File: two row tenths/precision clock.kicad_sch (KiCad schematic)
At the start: 56 parts, among them P1 USB_C_Plug_USB2.0, P2 USB_C_Plug_USB2.0, Q1 MMBT3906, Q2 MMBT3906

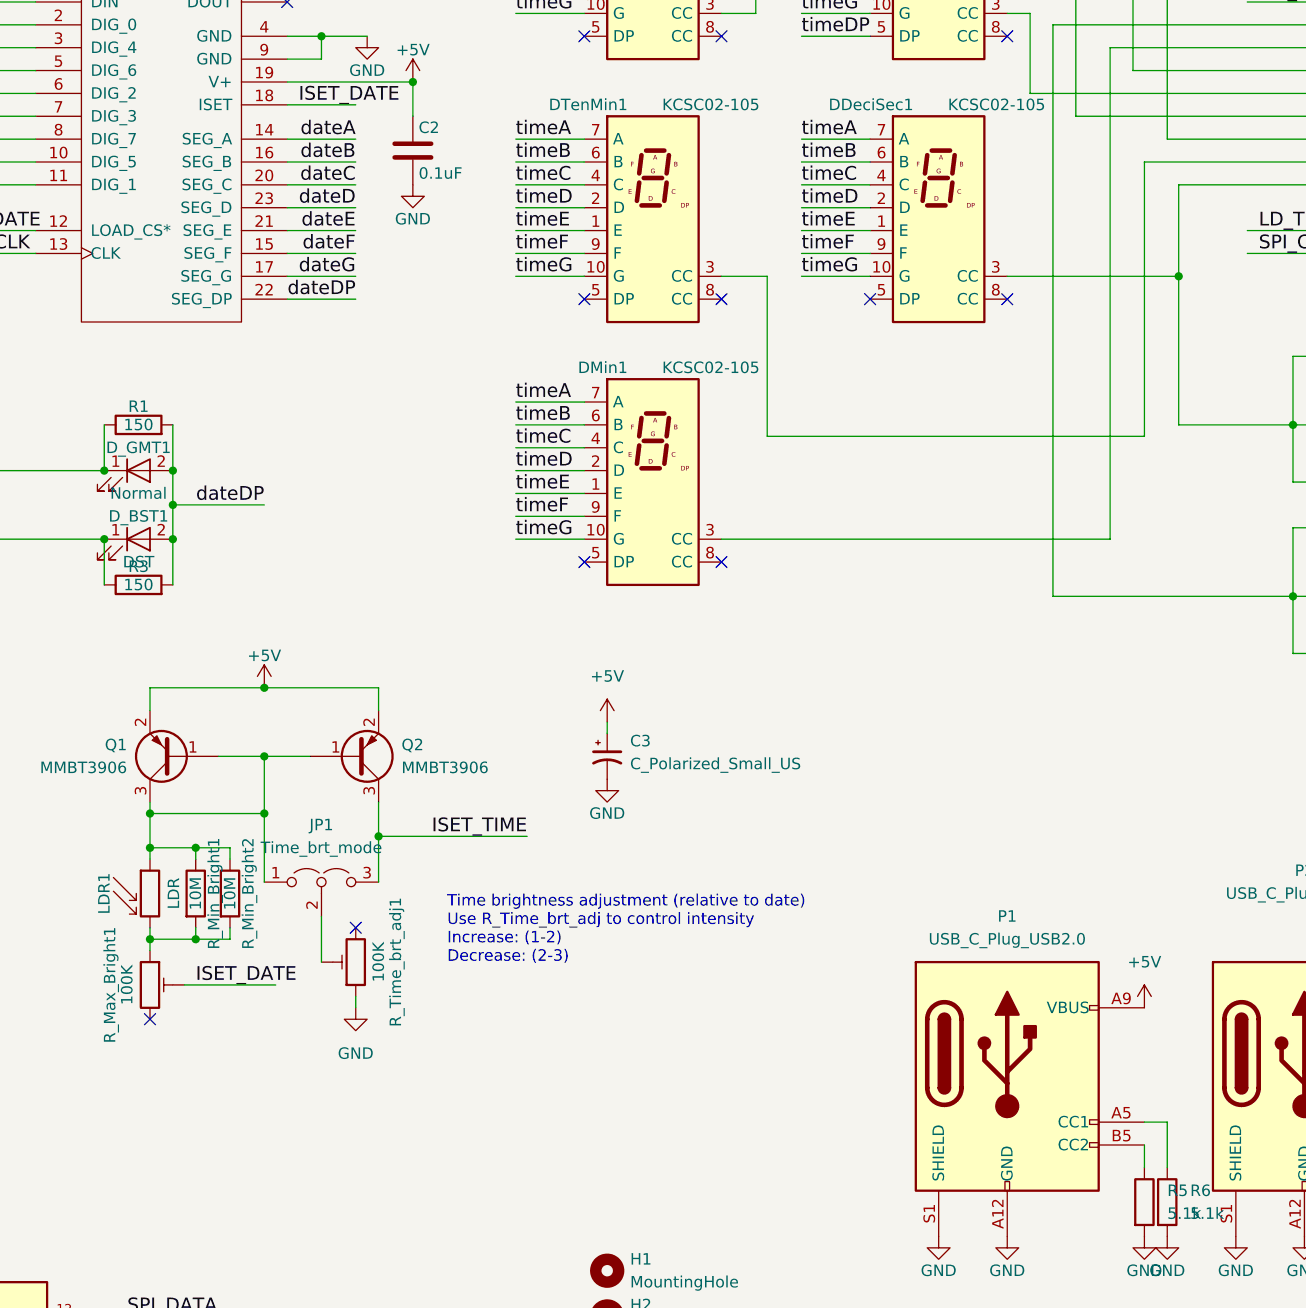
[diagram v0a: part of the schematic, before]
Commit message: Add resistor so we don't short Q2
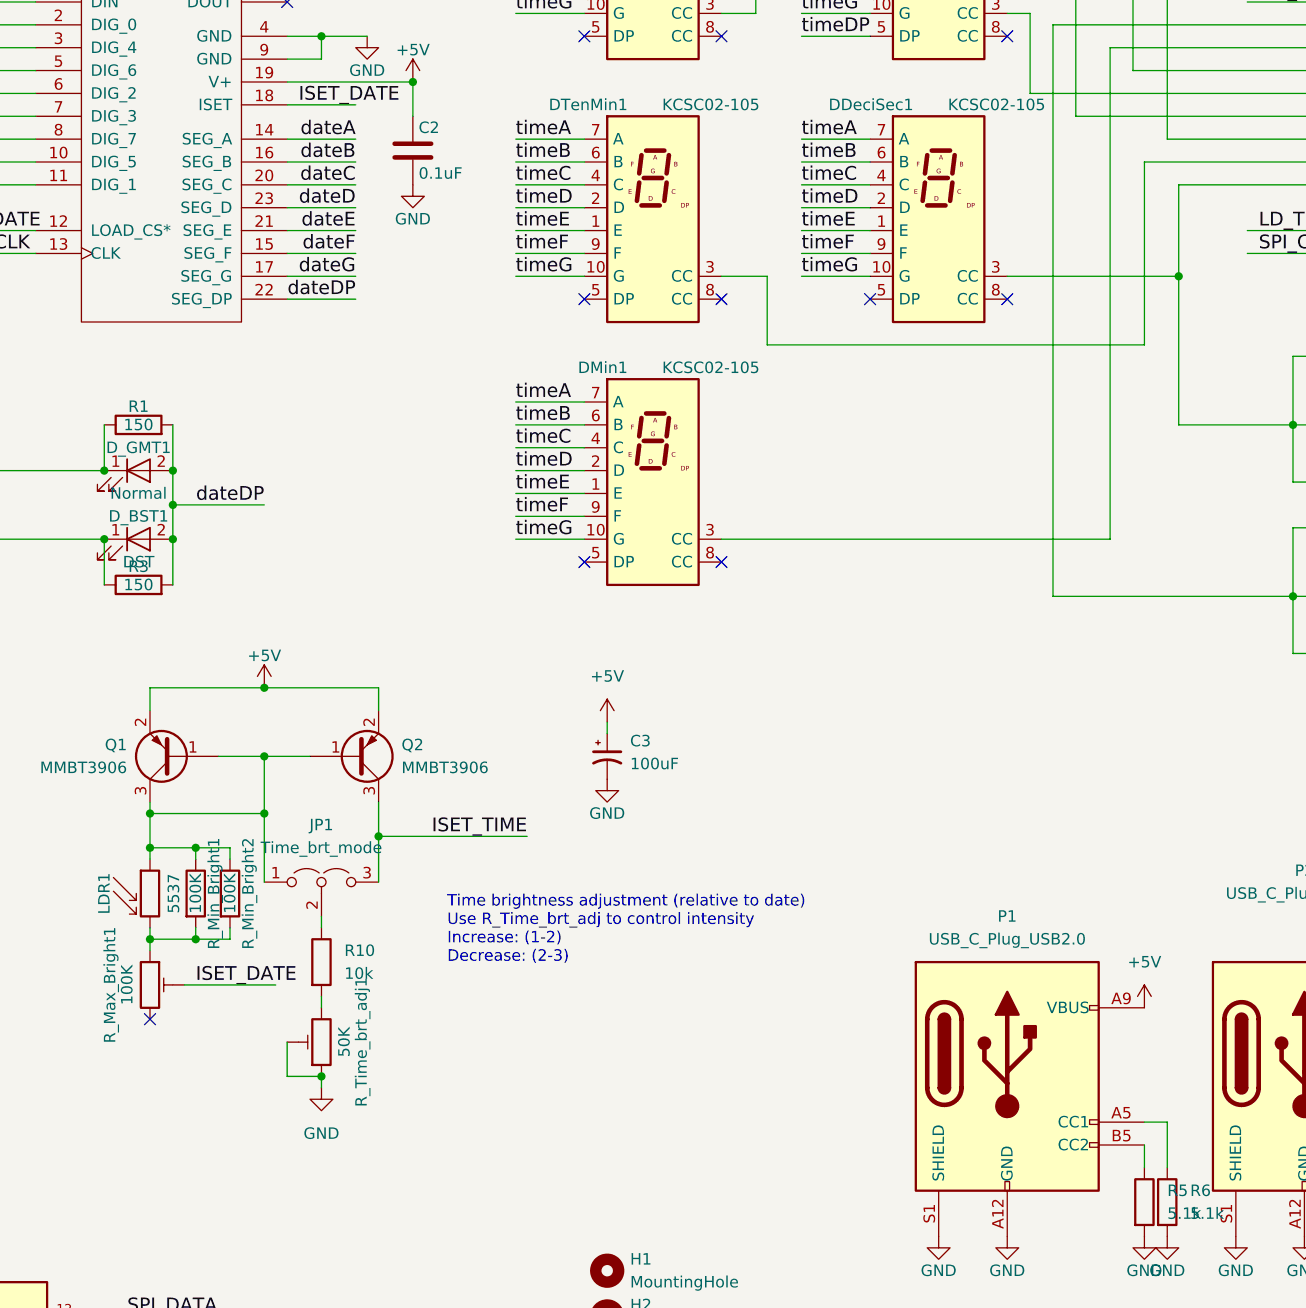
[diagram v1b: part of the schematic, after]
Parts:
- added R10: 10k, Resistor_SMD:R_1206_3216Metric, symbol Device:R
- C3: value C_Polarized_Small_US -> 100uF
- LDR1: value LDR -> 5537
- R_Min_Bright1, R_Min_Bright2: value 10M -> 100K
- R_Time_brt_adj1: value 100K -> 50K
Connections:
- net GND: now also R_Time_brt_adj1.2
- net at JP1.2 (C): now also R10.1; no longer R_Time_brt_adj1.2
- net at R_Time_brt_adj1.3: now also R10.2
- no-connect marks 59 -> 58
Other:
- moved on the sheet: R_Time_brt_adj1
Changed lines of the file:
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@@
 	)
 	(junction
+		(at 140.97 185.42)
+		(diameter 0)
+		(color 0 0 0 0)
+	)
+	(junction
 		(at 285.75 69.85)
 		(diameter 0)
@@
 	)
 	(no_connect
-		(at 144.78 168.91)
-	)
-	(no_connect
 		(at 63.5 146.05)
 	)
@@
 	(wire
 		(pts
-			(xy 50.8 133.35) (xy 50.8 158.75)
+			(xy 140.97 177.8) (xy 140.97 176.53)
 		)
 		(stroke
@@
 	(wire
 		(pts
-			(xy 63.5 120.65) (xy 55.88 120.65)
+			(xy 50.8 133.35) (xy 50.8 158.75)
 		)
 		(stroke
@@
 	(wire
 		(pts
-			(xy 190.5 96.52) (xy 190.5 114.3)
+			(xy 63.5 120.65) (xy 55.88 120.65)
 		)
 		(stroke
@@
 	(wire
 		(pts
-			(xy 140.97 167.64) (xy 140.97 172.72)
+			(xy 190.5 96.52) (xy 190.5 104.14)
 		)
 		(stroke
@@
 	(wire
 		(pts
-			(xy 232.41 83.82) (xy 232.41 114.3)
+			(xy 232.41 83.82) (xy 232.41 104.14)
 		)
 		(stroke
@@
 	(wire
 		(pts
+			(xy 137.16 181.61) (xy 137.16 185.42)
+		)
+		(stroke
+			(width 0)
+			(type default)
+		)
+	)
+	(wire
+		(pts
 			(xy 129.54 149.86) (xy 134.62 149.86)
 		)
@@
 	(wire
 		(pts
+			(xy 140.97 168.91) (xy 140.97 167.64)
+		)
+		(stroke
+			(width 0)
+			(type default)
+		)
+	)
+	(wire
+		(pts
 			(xy 137.16 69.85) (xy 140.97 69.85)
 		)
@@
 	(wire
 		(pts
+			(xy 137.16 185.42) (xy 140.97 185.42)
+		)
+		(stroke
+			(width 0)
+			(type default)
+		)
+	)
+	(wire
+		(pts
 			(xy 31.75 96.52) (xy 24.13 96.52)
 		)
@@
 	(wire
 		(pts
-			(xy 144.78 176.53) (xy 144.78 177.8)
+			(xy 140.97 185.42) (xy 140.97 186.69)
 		)
 		(stroke
@@
 	(wire
 		(pts
-			(xy 190.5 114.3) (xy 232.41 114.3)
+			(xy 190.5 104.14) (xy 232.41 104.14)
 		)
 		(stroke
@@
 			)
 		)
-		(property "Value" "LDR"
+		(property "Value" "5537"
 			(at 123.825 165.1 90)
 			(effects
@@
 			)
 		)
-		(property "Value" "10M"
+		(property "Value" "100K"
 			(at 127 165.1 90)
 			(effects
@@
 	(symbol
 		(lib_id "precision-clock-rescue:POT_TRIM")
-		(at 144.78 172.72 180)
+		(at 140.97 181.61 180)
 		(unit 1)
 		(exclude_from_sim no)
@@
 		(dnp no)
 		(property "Reference" "R_Time_brt_adj1"
-			(at 149.225 172.72 90)
+			(at 145.415 181.61 90)
 			(effects
 				(font
@@
 			)
 		)
-		(property "Value" "100K"
-			(at 147.32 172.72 90)
+		(property "Value" "50K"
+			(at 143.51 181.61 90)
 			(effects
 				(font
@@
 		)
 		(property "Footprint" "Potentiometer_THT:Potentiometer_Piher_PT-6-V_Vertical"
-			(at 144.78 172.72 0)
+			(at 140.97 181.61 0)
 			(effects
 				(font
@@
 		)
 		(property "Datasheet" ""
-			(at 144.78 172.72 0)
+			(at 140.97 181.61 0)
 			(effects
 				(font
@@
 		)
 		(property "Description" ""
-			(at 144.78 172.72 0)
+			(at 140.97 181.61 0)
 			(effects
 				(font
@@
 			)
 		)
-		(property "Value" "10M"
+		(property "Value" "100K"
 			(at 130.81 165.1 90)
 			(effects
@@
 	)
 	(symbol
+		(lib_id "Device:R")
+		(at 140.97 172.72 0)
+		(unit 1)
+		(exclude_from_sim no)
+		(in_bom yes)
+		(on_board yes)
+		(dnp no)
+		(fields_autoplaced yes)
+		(property "Reference" "R10"
+			(at 143.51 171.4499 0)
+			(effects
+				(font
+					(size 1.27 1.27)
+				)
+				(justify left)
+			)
+		)
+		(property "Value" "10k"
+			(at 143.51 173.9899 0)
+			(effects
+				(font
+					(size 1.27 1.27)
+				)
+				(justify left)
+			)
+		)
+		(property "Footprint" "Resistor_SMD:R_1206_3216Metric"
+			(at 139.192 172.72 90)
+			(effects
+				(font
+					(size 1.27 1.27)
+				)
+				(hide yes)
+			)
+		)
+		(property "Datasheet" "~"
+			(at 140.97 172.72 0)
+			(effects
+				(font
+					(size 1.27 1.27)
+				)
+				(hide yes)
+			)
+		)
+		(property "Description" "Resistor"
+			(at 140.97 172.72 0)
+			(effects
+				(font
+					(size 1.27 1.27)
+				)
+				(hide yes)
+			)
+		)
+		(pin "1"
+		)
+		(pin "2"
+		)
+		(instances
+			(project ""
+				(path "/a352d3ae-caca-4fe6-94e2-4912021cb238"
+					(reference "R10")
+					(unit 1)
+				)
+			)
+		)
+	)
+	(symbol
 		(lib_id "Connector:USB_C_Receptacle_PowerOnly_6P")
 		(at 250.19 185.42 0)
@@
 	(symbol
 		(lib_id "power:GND")
-		(at 144.78 177.8 0)
+		(at 140.97 186.69 0)
 		(unit 1)
 		(exclude_from_sim no)
@@
 		(fields_autoplaced yes)
 		(property "Reference" "#PWR010"
-			(at 144.78 184.15 0)
+			(at 140.97 193.04 0)
 			(effects
 				(font
@@
 		)
 		(property "Value" "GND"
-			(at 144.78 182.88 0)
+			(at 140.97 191.77 0)
 			(effects
 				(font
@@
 		)
 		(property "Footprint" ""
-			(at 144.78 177.8 0)
+			(at 140.97 186.69 0)
 			(effects
 				(font
@@
 		)
 		(property "Datasheet" ""
-			(at 144.78 177.8 0)
+			(at 140.97 186.69 0)
 			(effects
 				(font
@@
 		)
 		(property "Description" "Power symbol creates a global label with name \"GND\" , ground"
-			(at 144.78 177.8 0)
+			(at 140.97 186.69 0)
 			(effects
 				(font
@@
 			)
 		)
-		(property "Value" "C_Polarized_Small_US"
+		(property "Value" "100uF"
 			(at 175.26 150.6981 0)
 			(effects

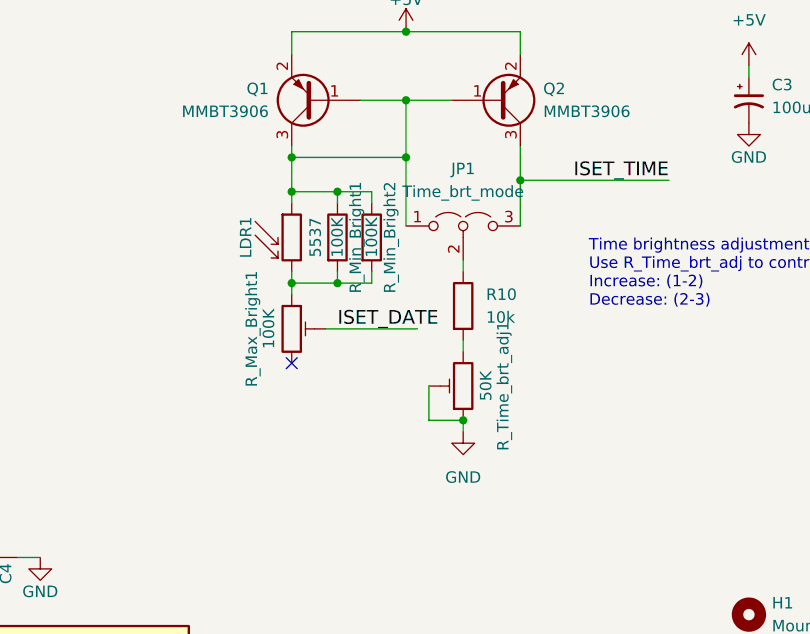
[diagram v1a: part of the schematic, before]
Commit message: More resistors for brightness tuning
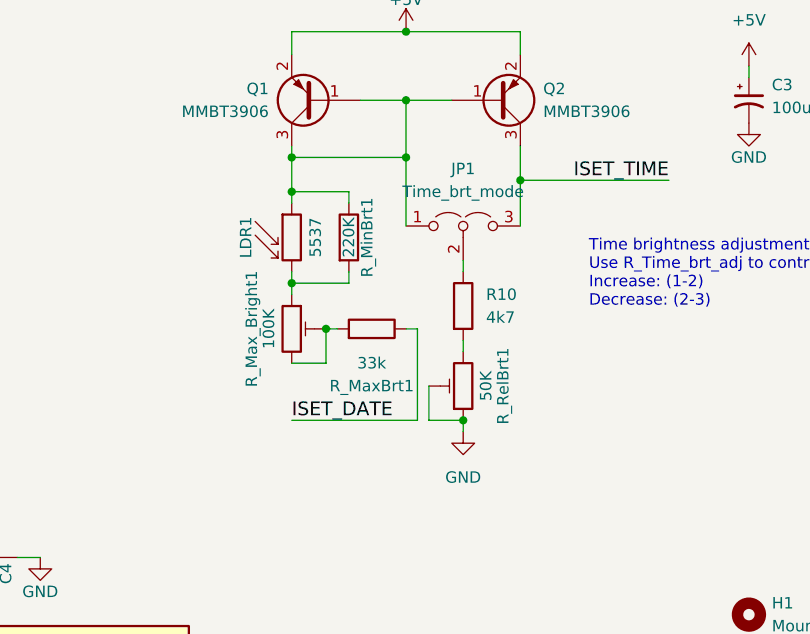
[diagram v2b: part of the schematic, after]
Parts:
- removed R_Min_Bright1: 100K, Resistor_THT:R_Axial_DIN0207_L6.3mm_D2.5mm_P7.62mm_Horizontal, symbol precision-clock-rescue:R
- added R_MaxBrt1: 33k, Resistor_SMD:R_1206_3216Metric, symbol Device:R
- R10: value 10k -> 4k7
- R_MinBrt1: renamed from R_Min_Bright2; value 100K -> 220K
- renumbered R_Time_brt_adj1 to R_RelBrt1
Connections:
- net ISET_DATE: now also R_MaxBrt1.1; no longer R_Max_Bright1.2
- net at R_Max_Bright1.3: now also R_Max_Bright1.2, R_MaxBrt1.2
- no-connect marks 58 -> 57
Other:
- moved on the sheet: R_MinBrt1
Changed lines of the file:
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@@
 	)
 	(junction
-		(at 127 160.02)
-		(diameter 0)
-		(color 0 0 0 0)
-	)
-	(junction
 		(at 83.82 125.73)
 		(diameter 0)
@@
 	)
 	(junction
-		(at 127 170.18)
+		(at 50.8 133.35)
 		(diameter 0)
 		(color 0 0 0 0)
 	)
 	(junction
-		(at 50.8 133.35)
+		(at 140.97 69.85)
 		(diameter 0)
 		(color 0 0 0 0)
 	)
 	(junction
-		(at 140.97 69.85)
+		(at 125.73 175.26)
 		(diameter 0)
 		(color 0 0 0 0)
@@
 	)
 	(no_connect
-		(at 121.92 179.07)
-	)
-	(no_connect
 		(at 31.75 99.06)
 	)
@@
 	(wire
 		(pts
+			(xy 135.89 185.42) (xy 121.92 185.42)
+		)
+		(stroke
+			(width 0)
+			(type default)
+		)
+	)
+	(wire
+		(pts
 			(xy 209.55 240.03) (xy 196.85 240.03)
 		)
@@
 	(wire
 		(pts
+			(xy 135.89 175.26) (xy 135.89 185.42)
+		)
+		(stroke
+			(width 0)
+			(type default)
+		)
+	)
+	(wire
+		(pts
 			(xy 121.92 168.91) (xy 121.92 170.18)
 		)
@@
 	(wire
 		(pts
-			(xy 127 160.02) (xy 130.81 160.02)
-		)
-		(stroke
-			(width 0)
-			(type default)
-		)
-	)
-	(wire
-		(pts
 			(xy 96.52 81.28) (xy 96.52 15.24)
 		)
@@
 	(wire
 		(pts
-			(xy 127 170.18) (xy 121.92 170.18)
+			(xy 121.92 170.18) (xy 128.27 170.18)
 		)
 		(stroke
@@
 	(wire
 		(pts
-			(xy 127 160.02) (xy 121.92 160.02)
+			(xy 121.92 160.02) (xy 128.27 160.02)
 		)
 		(stroke
@@
 	(wire
 		(pts
-			(xy 130.81 170.18) (xy 127 170.18)
+			(xy 135.89 175.26) (xy 134.62 175.26)
 		)
 		(stroke
@@
 	(wire
 		(pts
-			(xy 125.73 175.26) (xy 135.89 175.26)
-		)
-		(stroke
-			(width 0)
-			(type default)
-		)
-	)
-	(wire
-		(pts
 			(xy 147.32 154.94) (xy 147.32 158.75)
 		)
@@
 	(wire
 		(pts
-			(xy 127 161.29) (xy 127 160.02)
+			(xy 189.23 15.24) (xy 189.23 38.1)
 		)
 		(stroke
@@
 	(wire
 		(pts
-			(xy 189.23 15.24) (xy 189.23 38.1)
+			(xy 170.18 91.44) (xy 162.56 91.44)
 		)
 		(stroke
@@
 	(wire
 		(pts
-			(xy 170.18 91.44) (xy 162.56 91.44)
+			(xy 125.73 175.26) (xy 125.73 179.07)
 		)
 		(stroke
@@
 	(wire
 		(pts
-			(xy 236.22 113.03) (xy 248.92 113.03)
+			(xy 125.73 175.26) (xy 127 175.26)
 		)
 		(stroke
@@
 	(wire
 		(pts
-			(xy 31.75 158.75) (xy 24.13 158.75)
+			(xy 236.22 113.03) (xy 248.92 113.03)
 		)
 		(stroke
@@
 	(wire
 		(pts
-			(xy 63.5 59.69) (xy 55.88 59.69)
+			(xy 31.75 158.75) (xy 24.13 158.75)
 		)
 		(stroke
@@
 	(wire
 		(pts
-			(xy 127 168.91) (xy 127 170.18)
+			(xy 63.5 59.69) (xy 55.88 59.69)
 		)
 		(stroke
@@
 	(wire
 		(pts
-			(xy 130.81 168.91) (xy 130.81 170.18)
+			(xy 128.27 168.91) (xy 128.27 170.18)
 		)
 		(stroke
@@
 	(wire
 		(pts
+			(xy 125.73 179.07) (xy 121.92 179.07)
+		)
+		(stroke
+			(width 0)
+			(type default)
+		)
+	)
+	(wire
+		(pts
 			(xy 281.94 77.47) (xy 289.56 77.47)
 		)
@@
 	(wire
 		(pts
-			(xy 130.81 161.29) (xy 130.81 160.02)
+			(xy 128.27 161.29) (xy 128.27 160.02)
 		)
 		(stroke
@@
 	)
 	(label "ISET_DATE"
-		(at 127 175.26 0)
+		(at 121.92 185.42 0)
 		(fields_autoplaced yes)
 		(effects
@@
 	)
 	(symbol
-		(lib_id "precision-clock-rescue:R")
-		(at 127 165.1 0)
-		(unit 1)
-		(exclude_from_sim no)
-		(in_bom yes)
-		(on_board yes)
-		(dnp no)
-		(property "Reference" "R_Min_Bright1"
-			(at 129.032 165.1 90)
-			(effects
-				(font
-					(size 1.27 1.27)
-				)
-			)
-		)
-		(property "Value" "100K"
-			(at 127 165.1 90)
-			(effects
-				(font
-					(size 1.27 1.27)
-				)
-			)
-		)
-		(property "Footprint" "Resistor_THT:R_Axial_DIN0207_L6.3mm_D2.5mm_P7.62mm_Horizontal"
-			(at 125.222 165.1 90)
-			(effects
-				(font
-					(size 1.27 1.27)
-				)
-				(hide yes)
-			)
-		)
-		(property "Datasheet" ""
-			(at 127 165.1 0)
-			(effects
-				(font
-					(size 1.27 1.27)
-				)
-				(hide yes)
-			)
-		)
-		(property "Description" ""
-			(at 127 165.1 0)
-			(effects
-				(font
-					(size 1.27 1.27)
-				)
-				(hide yes)
-			)
-		)
-		(pin "2"
-		)
-		(pin "1"
-		)
-		(instances
-			(project ""
-				(path "/a352d3ae-caca-4fe6-94e2-4912021cb238"
-					(reference "R_Min_Bright1")
-					(unit 1)
-				)
-			)
-		)
-	)
-	(symbol
 		(lib_id "precision-clock-rescue:NEO6MV2")
 		(at 231.14 213.36 0)
@@
 		(on_board yes)
 		(dnp no)
-		(property "Reference" "R_Time_brt_adj1"
+		(property "Reference" "R_RelBrt1"
 			(at 145.415 181.61 90)
 			(effects
@@
 			(project "precision clock"
 				(path "/a352d3ae-caca-4fe6-94e2-4912021cb238"
-					(reference "R_Time_brt_adj1")
+					(reference "R_RelBrt1")
 					(unit 1)
 				)
@@
 	(symbol
 		(lib_id "precision-clock-rescue:R")
-		(at 130.81 165.1 0)
+		(at 128.27 165.1 0)
 		(unit 1)
 		(exclude_from_sim no)
@@
 		(on_board yes)
 		(dnp no)
-		(property "Reference" "R_Min_Bright2"
-			(at 132.842 165.1 90)
+		(property "Reference" "R_MinBrt1"
+			(at 130.302 165.1 90)
 			(effects
 				(font
@@
 			)
 		)
-		(property "Value" "100K"
-			(at 130.81 165.1 90)
+		(property "Value" "220K"
+			(at 128.27 165.1 90)
 			(effects
 				(font
@@
 		)
 		(property "Footprint" "Resistor_SMD:R_1206_3216Metric"
-			(at 129.032 165.1 90)
+			(at 126.492 165.1 90)
 			(effects
 				(font
@@
 		)
 		(property "Datasheet" ""
-			(at 130.81 165.1 0)
+			(at 128.27 165.1 0)
 			(effects
 				(font
@@
 		)
 		(property "Description" ""
-			(at 130.81 165.1 0)
+			(at 128.27 165.1 0)
 			(effects
 				(font
@@
 			(project "precision clock"
 				(path "/a352d3ae-caca-4fe6-94e2-4912021cb238"
-					(reference "R_Min_Bright2")
+					(reference "R_MinBrt1")
 					(unit 1)
 				)
@@
 	)
 	(symbol
+		(lib_id "Device:R")
+		(at 130.81 175.26 270)
+		(mirror x)
+		(unit 1)
+		(exclude_from_sim no)
+		(in_bom yes)
+		(on_board yes)
+		(dnp no)
+		(property "Reference" "R_MaxBrt1"
+			(at 130.81 181.61 90)
+			(effects
+				(font
+					(size 1.27 1.27)
+				)
+			)
+		)
+		(property "Value" "33k"
+			(at 130.81 179.07 90)
+			(effects
+				(font
+					(size 1.27 1.27)
+				)
+			)
+		)
+		(property "Footprint" "Resistor_SMD:R_1206_3216Metric"
+			(at 130.81 177.038 90)
+			(effects
+				(font
+					(size 1.27 1.27)
+				)
+				(hide yes)
+			)
+		)
+		(property "Datasheet" "~"
+			(at 130.81 175.26 0)
+			(effects
+				(font
+					(size 1.27 1.27)
+				)
+				(hide yes)
+			)
+		)
+		(property "Description" "Resistor"
+			(at 130.81 175.26 0)
+			(effects
+				(font
+					(size 1.27 1.27)
+				)
+				(hide yes)
+			)
+		)
+		(pin "1"
+		)
+		(pin "2"
+		)
+		(instances
+			(project "precision clock"
+				(path "/a352d3ae-caca-4fe6-94e2-4912021cb238"
+					(reference "R_MaxBrt1")
+					(unit 1)
+				)
+			)
+		)
+	)
+	(symbol
 		(lib_id "precision-clock-rescue:GND")
 		(at 209.55 203.2 0)
@@
 			)
 		)
-		(property "Value" "10k"
+		(property "Value" "4k7"
 			(at 143.51 173.9899 0)
 			(effects
